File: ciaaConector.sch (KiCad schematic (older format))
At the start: 3 parts, among them P1 PWR_JUMPER

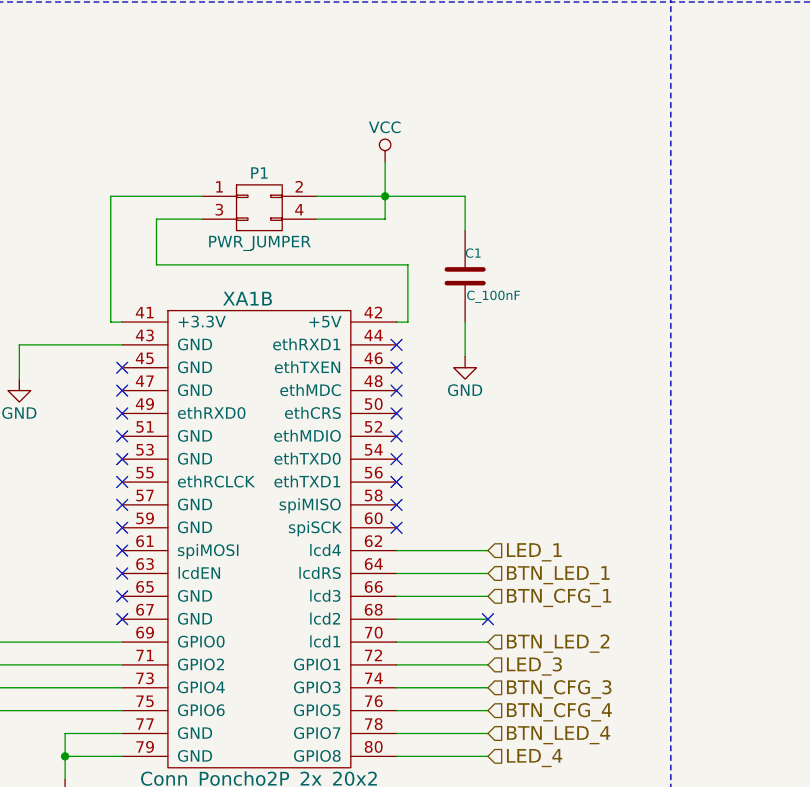
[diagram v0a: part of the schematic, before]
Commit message: Version 1 practicamente terminada de poncho Simon con EDU CIAA.
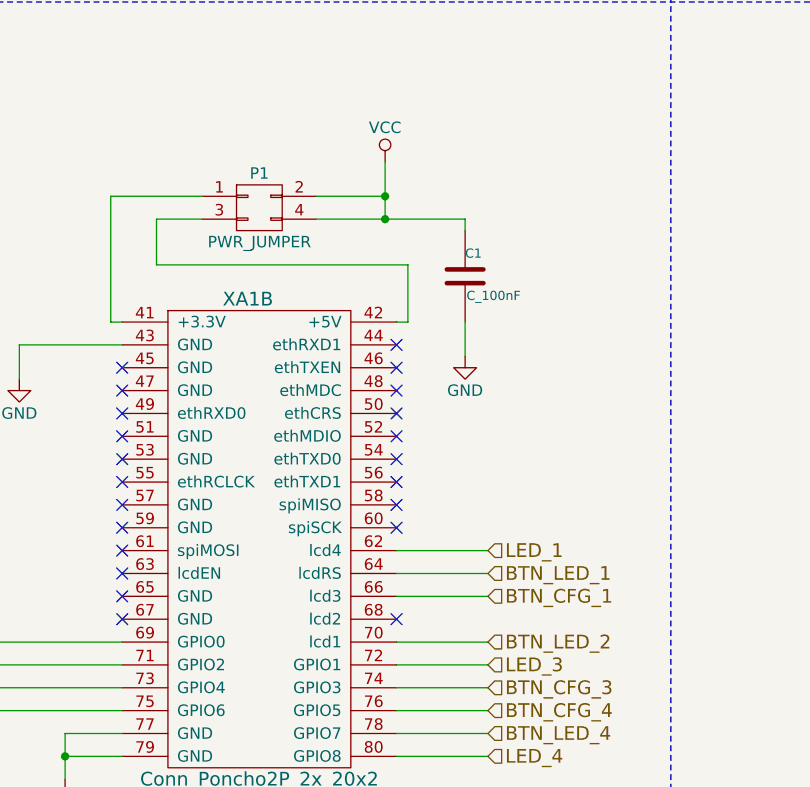
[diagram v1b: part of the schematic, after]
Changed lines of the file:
@@
 NoConn ~ 4850 3550
 NoConn ~ 4850 3650
-NoConn ~ 5250 4050
+NoConn ~ 4850 4050
 NoConn ~ 3650 4050
 NoConn ~ 3650 3950
@@
 	1    0    0    -1
 $EndComp
-Wire Wire Line
-	4800 2300 4500 2300
-Wire Wire Line
-	2900 4150 3650 4150
-Wire Wire Line
-	2900 4250 3650 4250
-Wire Wire Line
-	2900 4350 3650 4350
-Wire Wire Line
-	4850 4650 5250 4650
-Wire Wire Line
-	5250 4550 4850 4550
-Wire Wire Line
-	4850 4450 5250 4450
-Wire Wire Line
-	5250 4350 4850 4350
-Wire Wire Line
-	4850 4250 5250 4250
-Wire Wire Line
-	5250 4150 4850 4150
-Wire Wire Line
-	4850 4050 5250 4050
-Wire Wire Line
-	5250 3950 4850 3950
-Wire Wire Line
-	4850 3750 5250 3750
-Wire Wire Line
-	4850 2750 4900 2750
-Wire Wire Line
-	4900 2750 4900 2500
-Wire Wire Line
-	4900 2500 3800 2500
-Wire Wire Line
-	3800 2500 3800 2300
-Wire Wire Line
-	3800 2300 4000 2300
-Wire Wire Line
-	3650 2750 3600 2750
-Wire Wire Line
-	3600 2750 3600 2200
-Wire Wire Line
-	3600 2200 4000 2200
-Wire Wire Line
-	3200 2850 3200 3000
-Wire Wire Line
-	4800 2050 4800 2300
-Wire Wire Line
-	3650 2850 3200 2850
-Wire Wire Line
-	3650 4450 2900 4450
-Wire Notes Line
-	1950 1050 1950 5450
-Wire Notes Line
-	1950 5450 9850 5450
-Wire Notes Line
-	9850 5450 9850 1050
-Wire Notes Line
-	9850 1050 1950 1050
-Wire Notes Line
-	1950 1200 9850 1200
-Wire Notes Line
-	9850 1350 1950 1350
-Wire Notes Line
-	6050 1200 6050 5450
-Wire Wire Line
-	3650 4650 3400 4650
-Wire Wire Line
-	3400 4550 3400 4750
-Wire Wire Line
-	3650 4550 3400 4550
-Connection ~ 3400 4650
-Wire Wire Line
-	5250 3850 4850 3850
-Connection ~ 4800 2200
-Wire Wire Line
-	4500 2200 5150 2200
 $Comp
 L GND #PWR029
@@
 	1    0    0    -1
 $EndComp
-Wire Wire Line
-	5150 2750 5150 2900
 $Comp
 L C_100nF C1
@@
 $EndComp
 Wire Wire Line
-	5150 2200 5150 2350
+	2900 4150 3650 4150
+Wire Wire Line
+	2900 4250 3650 4250
+Wire Wire Line
+	2900 4350 3650 4350
+Wire Wire Line
+	4850 4650 5250 4650
+Wire Wire Line
+	5250 4550 4850 4550
+Wire Wire Line
+	4850 4450 5250 4450
+Wire Wire Line
+	5250 4350 4850 4350
+Wire Wire Line
+	4850 4250 5250 4250
+Wire Wire Line
+	5250 4150 4850 4150
+Wire Wire Line
+	5250 3950 4850 3950
+Wire Wire Line
+	4850 3750 5250 3750
+Wire Wire Line
+	4850 2750 4900 2750
+Wire Wire Line
+	4900 2750 4900 2500
+Wire Wire Line
+	4900 2500 3800 2500
+Wire Wire Line
+	3800 2500 3800 2300
+Wire Wire Line
+	3800 2300 4000 2300
+Wire Wire Line
+	3650 2750 3600 2750
+Wire Wire Line
+	3600 2750 3600 2200
+Wire Wire Line
+	3600 2200 4000 2200
+Wire Wire Line
+	3200 2850 3200 3000
+Wire Wire Line
+	3650 2850 3200 2850
+Wire Wire Line
+	3650 4450 2900 4450
+Wire Notes Line
+	1950 1050 1950 5450
+Wire Notes Line
+	1950 5450 9850 5450
+Wire Notes Line
+	9850 5450 9850 1050
+Wire Notes Line
+	9850 1050 1950 1050
+Wire Notes Line
+	1950 1200 9850 1200
+Wire Notes Line
+	9850 1350 1950 1350
+Wire Notes Line
+	6050 1200 6050 5450
+Wire Wire Line
+	3650 4650 3400 4650
+Wire Wire Line
+	3400 4550 3400 4750
+Wire Wire Line
+	3650 4550 3400 4550
+Connection ~ 3400 4650
+Wire Wire Line
+	5250 3850 4850 3850
+Wire Wire Line
+	5150 2750 5150 2900
+Wire Wire Line
+	4500 2200 4800 2200
+Wire Wire Line
+	4800 2300 4800 2050
+Wire Wire Line
+	4500 2300 5150 2300
+Connection ~ 4800 2200
+Wire Wire Line
+	5150 2300 5150 2350
+Connection ~ 4800 2300
 $EndSCHEMATC

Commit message: Version luego de cambiar los pines y agregar dos resistencias de puentes.@
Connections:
- net BTN_CFG_1: now also XA1.62 (lcd4); no longer XA1.66 (lcd3)
- net BTN_CFG_2: now also XA1.64 (lcdRS); no longer XA1.69 (GPIO0)
- net BTN_CFG_3: now also XA1.76 (GPIO5); no longer XA1.74 (GPIO3)
- net BTN_CFG_4: now also XA1.80 (GPIO8); no longer XA1.76 (GPIO5)
- net BTN_LED_1: now also XA1.60 (spiSCK); no longer XA1.64 (lcdRS)
- net BTN_LED_2: now also XA1.66 (lcd3); no longer XA1.70 (lcd1)
- net BTN_LED_3: now also XA1.78 (GPIO7); no longer XA1.73 (GPIO4)
- net BTN_LED_4: now also XA1.75 (GPIO6); no longer XA1.78 (GPIO7)
- net LED_1: now also XA1.58 (spiMISO); no longer XA1.62 (lcd4)
- net LED_2: now also XA1.68 (lcd2); no longer XA1.71 (GPIO2)
- net LED_3: now also XA1.74 (GPIO3); no longer XA1.72 (GPIO1)
- net LED_4: now also XA1.73 (GPIO4); no longer XA1.80 (GPIO8)
- net PWM: now also XA1.49 (ethRXD0); no longer XA1.75 (GPIO6)
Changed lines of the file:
@@
 NoConn ~ 4850 3350
 NoConn ~ 4850 3450
-NoConn ~ 4850 3550
-NoConn ~ 4850 3650
-NoConn ~ 4850 4050
 NoConn ~ 3650 4050
 NoConn ~ 3650 3950
@@
 NoConn ~ 3650 3350
 NoConn ~ 3650 3250
-NoConn ~ 3650 3150
 NoConn ~ 3650 3050
 NoConn ~ 3650 2950
-Text HLabel 5250 3950 2    60   Input ~ 0
+Text HLabel 4850 3750 2    60   Input ~ 0
 BTN_CFG_1
-Text HLabel 2900 4150 0    60   Input ~ 0
+Text HLabel 4850 3850 2    60   Input ~ 0
 BTN_CFG_2
-Text HLabel 5250 4350 2    60   Input ~ 0
+Text HLabel 4850 4450 2    60   Input ~ 0
 BTN_CFG_3
-Text HLabel 5250 4450 2    60   Input ~ 0
+Text HLabel 4850 4650 2    60   Input ~ 0
 BTN_CFG_4
-Text HLabel 5250 4650 2    60   Input ~ 0
+Text HLabel 3650 4350 0    60   Input ~ 0
 LED_4
-Text HLabel 5250 4250 2    60   Input ~ 0
+Text HLabel 4850 4350 2    60   Input ~ 0
 LED_3
-Text HLabel 2900 4250 0    60   Input ~ 0
+Text HLabel 4850 4050 2    60   Input ~ 0
 LED_2
-Text HLabel 5250 3750 2    60   Input ~ 0
+Text HLabel 4850 3550 2    60   Input ~ 0
 LED_1
-Text HLabel 5250 4550 2    60   Input ~ 0
+Text HLabel 3650 4450 0    60   Input ~ 0
 BTN_LED_4
-Text HLabel 2900 4350 0    60   Input ~ 0
+Text HLabel 4850 4550 2    60   Input ~ 0
 BTN_LED_3
-Text HLabel 5250 4150 2    60   Input ~ 0
+Text HLabel 4850 3950 2    60   Input ~ 0
 BTN_LED_2
-Text HLabel 5250 3850 2    60   Input ~ 0
+Text HLabel 4850 3650 2    60   Input ~ 0
 BTN_LED_1
-Text HLabel 2900 4450 0    60   Input ~ 0
+Text HLabel 3650 3150 0    60   Input ~ 0
 PWM
 $Comp
@@
 $EndComp
 Wire Wire Line
-	2900 4150 3650 4150
-Wire Wire Line
-	2900 4250 3650 4250
-Wire Wire Line
-	2900 4350 3650 4350
-Wire Wire Line
-	4850 4650 5250 4650
-Wire Wire Line
-	5250 4550 4850 4550
-Wire Wire Line
-	4850 4450 5250 4450
-Wire Wire Line
-	5250 4350 4850 4350
-Wire Wire Line
-	4850 4250 5250 4250
-Wire Wire Line
-	5250 4150 4850 4150
-Wire Wire Line
-	5250 3950 4850 3950
-Wire Wire Line
-	4850 3750 5250 3750
-Wire Wire Line
 	4850 2750 4900 2750
 Wire Wire Line
@@
 Wire Wire Line
 	3650 2850 3200 2850
-Wire Wire Line
-	3650 4450 2900 4450
 Wire Notes Line
 	1950 1050 1950 5450
@@
 Connection ~ 3400 4650
 Wire Wire Line
-	5250 3850 4850 3850
-Wire Wire Line
 	5150 2750 5150 2900
 Wire Wire Line
@@
 	5150 2300 5150 2350
 Connection ~ 4800 2300
+NoConn ~ 3650 4250
+NoConn ~ 3650 4150
+NoConn ~ 4850 4150
+NoConn ~ 4850 4250
 $EndSCHEMATC
